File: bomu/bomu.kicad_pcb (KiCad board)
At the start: 6 copper layers, 13 x 9.4 mm, 33 parts, among them U1 NRF52840-CKAA-R7

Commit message: PCB design edits
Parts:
- TP1, TP10, TP3, TP4, TP5, TP6, TP7, TP9: value TestPoint -> DNP
- USB1: value USB-A-INSERT -> DNP
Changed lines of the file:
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@@
       (effects (font (size 1 1) (thickness 0.15)) (justify mirror))
     )
-    (fp_text value TestPoint (at 0 -1.55) (layer B.Fab) hide
+    (fp_text value DNP (at 0 -1.55) (layer B.Fab) hide
       (effects (font (size 1 1) (thickness 0.15)) (justify mirror))
     )
@@
       (effects (font (size 1 1) (thickness 0.15)) (justify mirror))
     )
-    (fp_text value TestPoint (at 0 -1.55) (layer B.Fab) hide
+    (fp_text value DNP (at 0 -1.55) (layer B.Fab) hide
       (effects (font (size 1 1) (thickness 0.15)) (justify mirror))
     )
@@
       (effects (font (size 1 1) (thickness 0.15)) (justify mirror))
     )
-    (fp_text value TestPoint (at 0 -1.55) (layer B.Fab) hide
+    (fp_text value DNP (at 0 -1.55) (layer B.Fab) hide
       (effects (font (size 1 1) (thickness 0.15)) (justify mirror))
     )
@@
       (effects (font (size 1 1) (thickness 0.15)))
     )
-    (fp_text value TestPoint (at 0 1.55) (layer F.Fab) hide
+    (fp_text value DNP (at 0 1.55) (layer F.Fab) hide
       (effects (font (size 1 1) (thickness 0.15)))
     )
@@
       (effects (font (size 1 1) (thickness 0.15)))
     )
-    (fp_text value TestPoint (at 0 1.55 90) (layer F.Fab) hide
+    (fp_text value DNP (at 0 1.55 90) (layer F.Fab) hide
       (effects (font (size 1 1) (thickness 0.15)))
     )
@@
       (effects (font (size 1 1) (thickness 0.15)))
     )
-    (fp_text value TestPoint (at 0 1.55 90) (layer F.Fab) hide
+    (fp_text value DNP (at 0 1.55 90) (layer F.Fab) hide
       (effects (font (size 1 1) (thickness 0.15)))
     )
@@
       (effects (font (size 1 1) (thickness 0.15)))
     )
-    (fp_text value TestPoint (at 0 1.55 90) (layer F.Fab) hide
+    (fp_text value DNP (at 0 1.55 90) (layer F.Fab) hide
       (effects (font (size 1 1) (thickness 0.15)))
     )
@@
       (effects (font (size 1 1) (thickness 0.15)))
     )
-    (fp_text value TestPoint (at 0 1.55 90) (layer F.Fab) hide
+    (fp_text value DNP (at 0 1.55 90) (layer F.Fab) hide
       (effects (font (size 1 1) (thickness 0.15)))
     )
@@
       (effects (font (size 1 1) (thickness 0.15)))
     )
-    (fp_text value USB-A-INSERT (at -0.254 -6.985) (layer F.Fab) hide
+    (fp_text value DNP (at -0.254 -6.985) (layer F.Fab) hide
       (effects (font (size 1 1) (thickness 0.15)))
     )

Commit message: Latest changes to the schematic and pcb
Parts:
- added C_RF2: DNP, Capacitor_SMD:C_0201_0603Metric, B.Cu at (141.3, 140.0)
- added C_RF3: DNP, Capacitor_SMD:C_0201_0603Metric, B.Cu at (143.0, 139.5)
- added L3: DNP, Inductor_SMD:L_0201_0603Metric, B.Cu at (140.4, 140.3)
- added TP11: DNP, TestPoint:TestPoint_Pad_D1.0mm, F.Cu at (141.3, 133.9)
- added TP12: DNP, TestPoint:TestPoint_Pad_D1.0mm, F.Cu at (142.2, 133.9)
- C10, C11, C15, C8, C9: footprint Capacitor_SMD:C_0201_0603Metric -> Capacitor_SMD:C_0402_1005Metric
- C4, C5: value C_Small -> 12pF
- C6, C7: value C_Small -> 6pF
- TP8: value TestPoint -> DNP
- moved C_RF1 1.16 mm to (139.4, 140.0), turned to 90 degrees
- moved C1 0.72 mm to (136.6, 139.9), turned to 45 degrees
- moved C8 0.69 mm to (133.6, 133.8)
- moved R1 0.56 mm to (133.1, 140.8)
- moved C14 0.53 mm to (139.2, 138.9)
- moved C9 0.40 mm to (134.6, 133.6)
- moved C4 0.36 mm to (139.4, 138.2), turned to 180 degrees
- moved C5 0.28 mm to (139.3, 134.8)
- moved C10 0.24 mm to (135.5, 133.6)
- moved C11 0.13 mm to (136.3, 133.6)
- moved L1 0.08 mm to (136.2, 138.9)
- moved C15 0.08 mm to (137.3, 138.9)
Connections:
- C_RF1 pad 1: Net-(ANT1-PadFEED) -> Net-(C_RF1-Pad1)
- L2 pad 1: Net-(ANT1-PadFEED) -> Net-(C_RF1-Pad1)
- U1 pad E2: Net-(U1-PadE2) -> /NFC-
- U1 pad F1: Net-(U1-PadF1) -> /NFC+
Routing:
- net /NFC-: track 0.00 -> 8.41 mm, vias 0 -> 2
- net /NFC+: track 0.00 -> 8.02 mm, vias 0 -> 2
- net Net-(ANT1-PadFEED): track 7.30 -> 4.15 mm
- net Net-(C_RF1-Pad1): track 0.00 -> 2.51 mm
- net GND: track 60.2 -> 62.5 mm, vias 327 -> 334
- net +3V0: track 28.5 -> 30.0 mm
- net VBUS: track 4.48 -> 3.92 mm

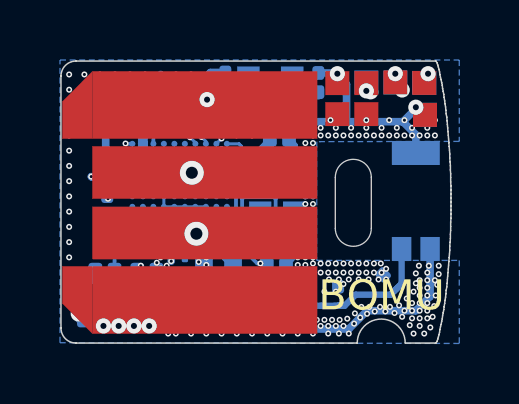
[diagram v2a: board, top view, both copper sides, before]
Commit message: Tonight's work on bomu. Added LC filter to VDD3P3 pins
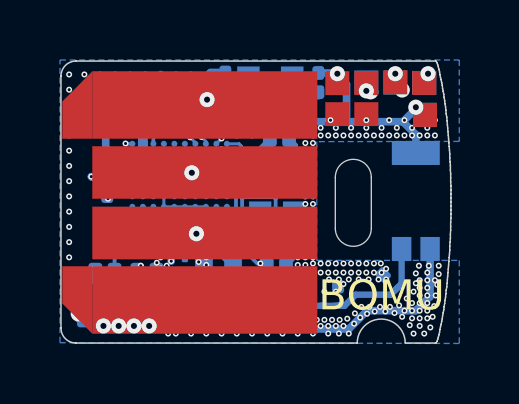
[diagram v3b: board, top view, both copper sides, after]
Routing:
- net +3V0: track 30.0 -> 29.4 mm

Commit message: Latest work on BOMU design
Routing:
- added copper zone on In4.Cu, net GND
- removed copper zone on In4.Cu.GND, net GND
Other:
- net class Default removed
